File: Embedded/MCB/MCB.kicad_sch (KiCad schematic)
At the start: 23 parts, among them J1 USB, J2 Power, J3 MicroSD, J4 GPIO Pair 0, J5 GPIO Pair 1, U1 Sensored, U2 Expansion, U3 Comms Link Expansion, U4 AP7366-33W5-7

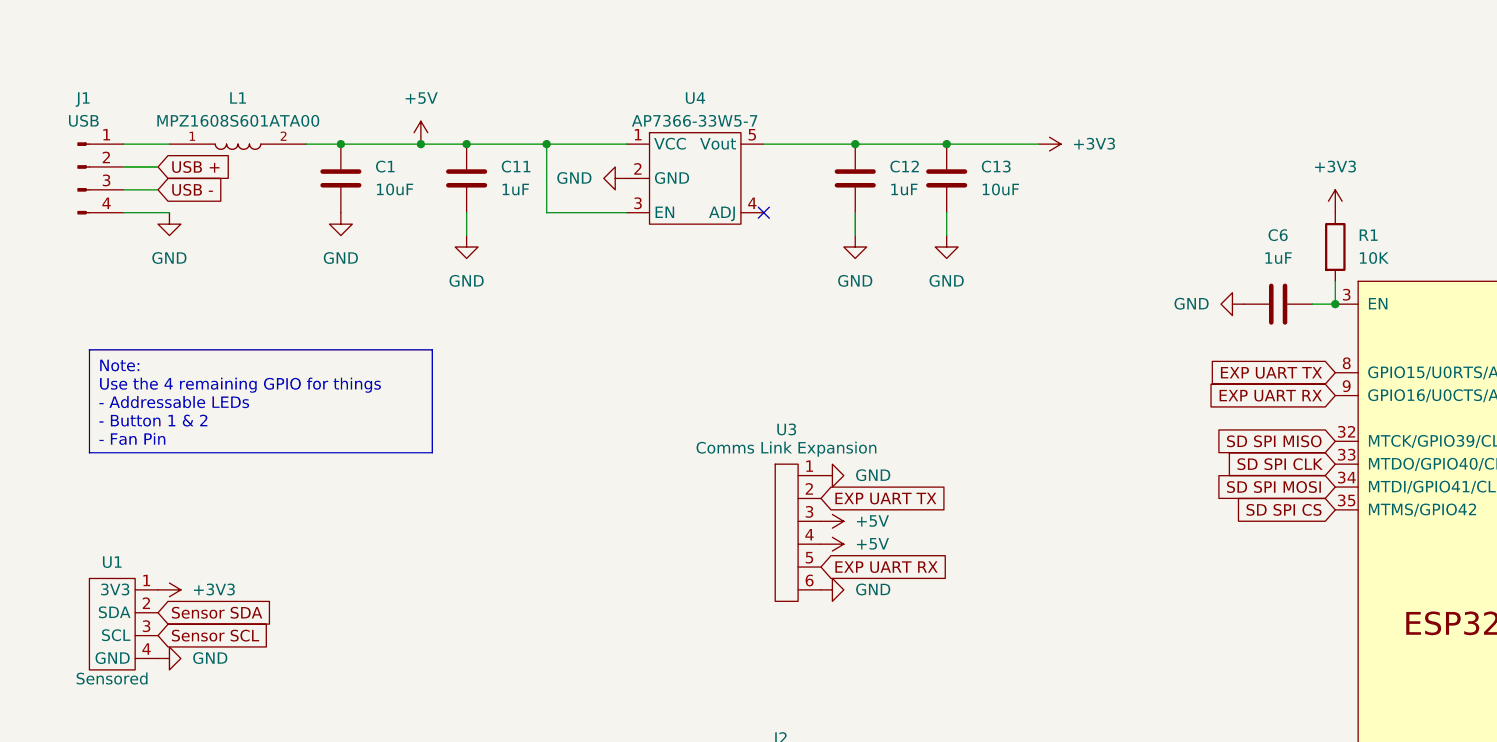
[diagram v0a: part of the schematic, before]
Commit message: Added USB-2WComms Solder Bridge
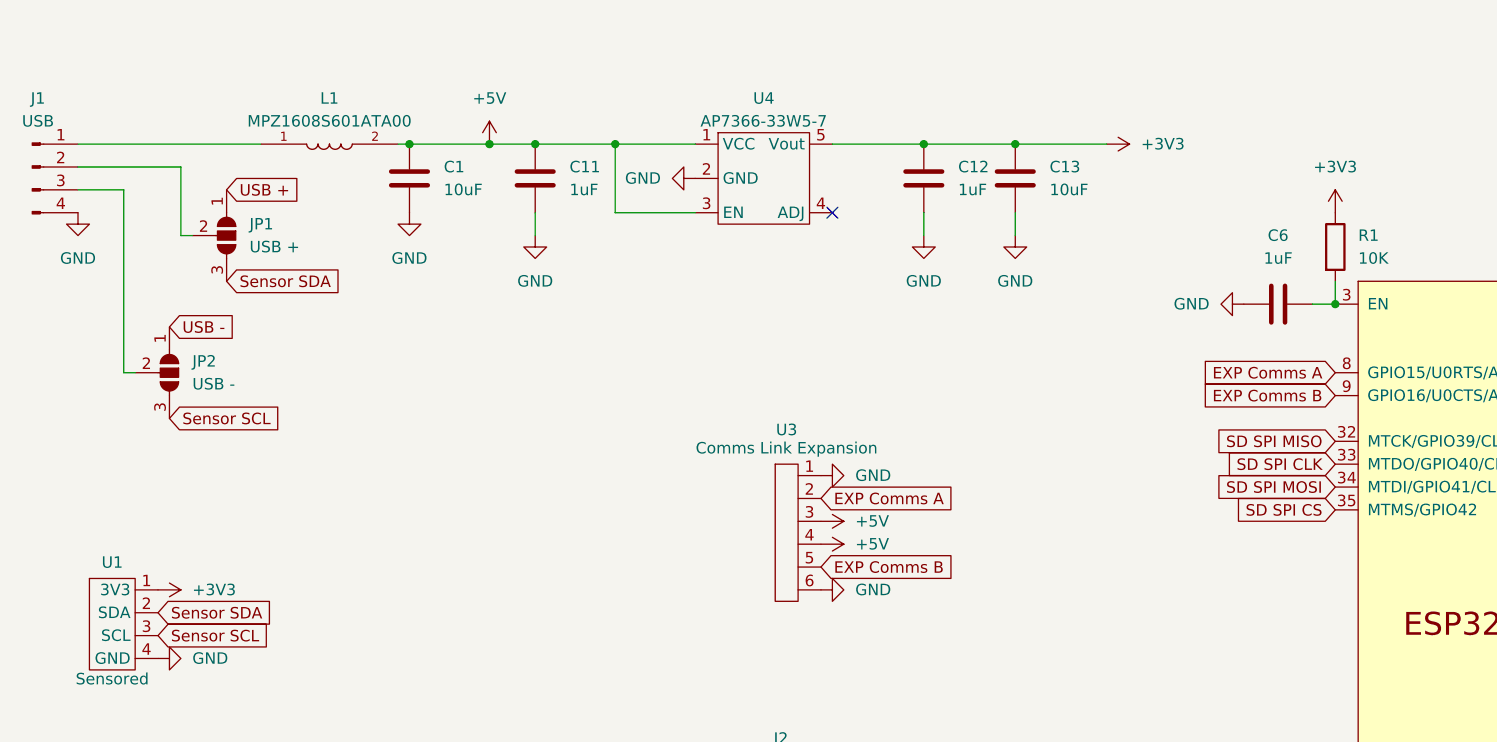
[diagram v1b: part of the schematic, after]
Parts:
- added JP1: USB +, Jumper:SolderJumper-3_P1.3mm_Open_RoundedPad1.0x1.5mm, symbol Jumper:SolderJumper_3_Open
- added JP2: USB -, Jumper:SolderJumper-3_P1.3mm_Open_RoundedPad1.0x1.5mm, symbol Jumper:SolderJumper_3_Open
- C10: footprint Capacitor_SMD:C_0402_1005Metric_Pad0.74x0.62mm_HandSolder -> Capacitor_SMD:C_0603_1608Metric_Pad1.08x0.95mm_HandSolder
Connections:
- net Sensor SCL: now also JP2.3 (B)
- net Sensor SDA: now also JP1.3 (B)
- net USB +: now also JP1.1 (A); no longer J1.2 (Pin_2)
- net USB -: now also JP2.1 (A); no longer J1.3 (Pin_3)
- net EXP UART RX renamed EXP Comms B
- net EXP UART TX renamed EXP Comms A
- new net: J1.2 (Pin_2), JP1.2 (C)
- new net: J1.3 (Pin_3), JP2.2 (C)
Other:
- moved on the sheet: C1, C11, C12, C13, J1, L1, U4
